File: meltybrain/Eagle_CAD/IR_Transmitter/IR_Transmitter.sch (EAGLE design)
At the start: 14 parts, among them J1 AVR_SPI_PROG_3X2NS, Q1 BSS806N, Q2 FDN352AP, U1 LMH6612MAX/NOPB, U2 AP2210K-5.0TRG1

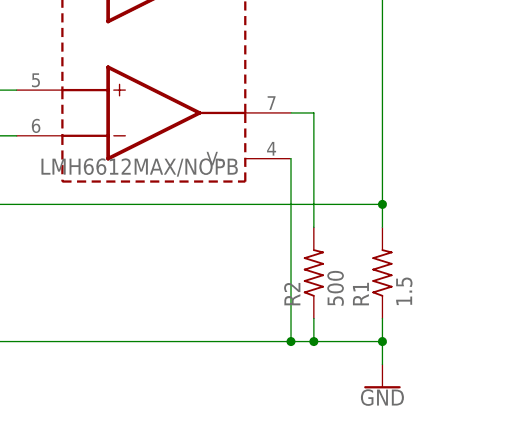
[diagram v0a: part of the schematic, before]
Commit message: Updated Hocki IR Receiver and removed extraneous file
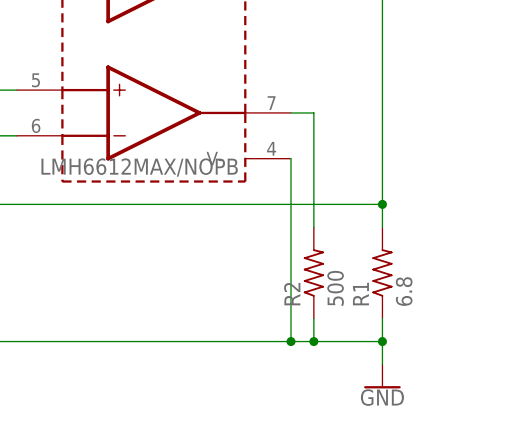
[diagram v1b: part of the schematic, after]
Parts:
- R1: value 1.5 -> 6.8; device rcl:R-US_R0402 -> rcl:R-US_R0603
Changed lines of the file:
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@@
 <layers>
 <layer number="1" name="Top" color="4" fill="1" visible="no" active="no"/>
-<layer number="2" name="Route2" color="1" fill="3" visible="no" active="no"/>
-<layer number="3" name="Route3" color="4" fill="3" visible="no" active="no"/>
-<layer number="4" name="Route4" color="1" fill="4" visible="no" active="no"/>
-<layer number="5" name="Route5" color="4" fill="4" visible="no" active="no"/>
-<layer number="6" name="Route6" color="1" fill="8" visible="no" active="no"/>
-<layer number="7" name="Route7" color="4" fill="8" visible="no" active="no"/>
-<layer number="8" name="Route8" color="1" fill="2" visible="no" active="no"/>
-<layer number="9" name="Route9" color="4" fill="2" visible="no" active="no"/>
-<layer number="10" name="Route10" color="1" fill="7" visible="no" active="no"/>
-<layer number="11" name="Route11" color="4" fill="7" visible="no" active="no"/>
-<layer number="12" name="Route12" color="1" fill="5" visible="no" active="no"/>
-<layer number="13" name="Route13" color="4" fill="5" visible="no" active="no"/>
-<layer number="14" name="Route14" color="1" fill="6" visible="no" active="no"/>
-<layer number="15" name="Route15" color="4" fill="6" visible="no" active="no"/>
 <layer number="16" name="Bottom" color="1" fill="1" visible="no" active="no"/>
 <layer number="17" name="Pads" color="2" fill="1" visible="no" active="no"/>
@@
 <part name="Q1" library="RoboJackets-Discrete" deviceset="BSS806N" device=""/>
 <part name="U1" library="Hocki_Library" deviceset="LMH6612MAX/NOPB" device=""/>
-<part name="R1" library="rcl" library_urn="urn:adsk.eagle:library:334" deviceset="R-US_" device="R0402" package3d_urn="urn:adsk.eagle:package:23547/3" value="1.5"/>
+<part name="R1" library="rcl" library_urn="urn:adsk.eagle:library:334" deviceset="R-US_" device="R0603" package3d_urn="urn:adsk.eagle:package:23555/3" value="6.8"/>
 <part name="GND1" library="SparkFun-PowerSymbols" library_urn="urn:adsk.eagle:library:530" deviceset="GND" device=""/>
 <part name="R2" library="rcl" library_urn="urn:adsk.eagle:library:334" deviceset="R-US_" device="R0603" package3d_urn="urn:adsk.eagle:package:23555/3" value="500"/>

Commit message: Finalized emitter board
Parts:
- R1: value 6.8 -> 1.5; device rcl:R-US_R0603 -> rcl:R-US_R0402
- renumbered U$1 to U3

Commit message: second round of gerbers
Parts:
- R1: device rcl:R-US_R0402 -> rcl:R-US_R0805
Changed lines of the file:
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@@
 <?xml version="1.0" encoding="utf-8"?>
 <!DOCTYPE eagle SYSTEM "eagle.dtd">
-<eagle version="9.5.2">
+<eagle version="9.6.2">
 <drawing>
 <settings>
@@
 <layers>
 <layer number="1" name="Top" color="4" fill="1" visible="no" active="no"/>
+<layer number="2" name="Route2" color="1" fill="3" visible="no" active="no"/>
+<layer number="3" name="Route3" color="4" fill="3" visible="no" active="no"/>
+<layer number="4" name="Route4" color="1" fill="4" visible="no" active="no"/>
+<layer number="5" name="Route5" color="4" fill="4" visible="no" active="no"/>
+<layer number="6" name="Route6" color="1" fill="8" visible="no" active="no"/>
+<layer number="7" name="Route7" color="4" fill="8" visible="no" active="no"/>
+<layer number="8" name="Route8" color="1" fill="2" visible="no" active="no"/>
+<layer number="9" name="Route9" color="4" fill="2" visible="no" active="no"/>
+<layer number="10" name="Route10" color="1" fill="7" visible="no" active="no"/>
+<layer number="11" name="Route11" color="4" fill="7" visible="no" active="no"/>
+<layer number="12" name="Route12" color="1" fill="5" visible="no" active="no"/>
+<layer number="13" name="Route13" color="4" fill="5" visible="no" active="no"/>
+<layer number="14" name="Route14" color="1" fill="6" visible="no" active="no"/>
+<layer number="15" name="Route15" color="4" fill="6" visible="no" active="no"/>
 <layer number="16" name="Bottom" color="1" fill="1" visible="no" active="no"/>
 <layer number="17" name="Pads" color="2" fill="1" visible="no" active="no"/>
@@
 <part name="GND5" library="SparkFun-PowerSymbols" library_urn="urn:adsk.eagle:library:530" deviceset="GND" device=""/>
 <part name="C2" library="rcl" library_urn="urn:adsk.eagle:library:334" deviceset="C-US" device="C0603" package3d_urn="urn:adsk.eagle:package:23616/2" value="0.1u"/>
-<part name="R1" library="rcl" library_urn="urn:adsk.eagle:library:334" deviceset="R-US_" device="R0402" package3d_urn="urn:adsk.eagle:package:23547/3" value="1.5"/>
+<part name="R1" library="rcl" library_urn="urn:adsk.eagle:library:334" deviceset="R-US_" device="R0805" package3d_urn="urn:adsk.eagle:package:23553/2" value="1.5"/>
 </parts>
 <sheets>
